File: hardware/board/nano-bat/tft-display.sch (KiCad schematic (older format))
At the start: 0 parts

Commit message: Adding larger microcontroller
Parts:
- added J?: Conn_2Rows-45Pins, symbol Connector_Generic:Conn_2Rows-45Pins
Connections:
- new net DB0: J?.28 (Pin_28)
- new net DB1: J?.27 (Pin_27)
- new net DB10: J?.18 (Pin_18)
- new net DB11: J?.17 (Pin_17)
- new net DB12: J?.16 (Pin_16)
- new net DB13: J?.15 (Pin_15)
- new net DB14: J?.14 (Pin_14)
- new net DB15: J?.13 (Pin_13)
- new net DB16: J?.12 (Pin_12)
- new net DB17: J?.11 (Pin_11)
- new net DB2: J?.26 (Pin_26)
- new net DB3: J?.25 (Pin_25)
- new net DB4: J?.24 (Pin_24)
- new net DB5: J?.23 (Pin_23)
- new net DB6: J?.22 (Pin_22)
- new net DB7: J?.21 (Pin_21)
- new net DB8: J?.20 (Pin_20)
- new net DB9: J?.19 (Pin_19)
- new net DOTCLK: J?.9 (Pin_9)
- new net ENABLE: J?.10 (Pin_10)
- new net FMARK: J?.35 (Pin_35)
- new net GND: J?.38 (Pin_38), J?.39 (Pin_39)
- new net HSYNC: J?.8 (Pin_8)
- new net IM0: J?.2 (Pin_2)
- new net IM1: J?.3 (Pin_3)
- new net IM2: J?.4 (Pin_4)
- new net IM3: J?.5 (Pin_5)
- new net LED_A: J?.40 (Pin_40)
- new net LED_K: J?.41 (Pin_41)
- new net RD: J?.31 (Pin_31)
- new net RESET: J?.6 (Pin_6)
- new net RS_SCL: J?.32 (Pin_32)
- new net SDI: J?.30 (Pin_30)
- new net SDO: J?.29 (Pin_29)
- new net VCC: J?.36 (Pin_36), J?.37 (Pin_37)
- new net VSYNC: J?.7 (Pin_7)
- new net WR: J?.33 (Pin_33)
- new net ~CS: J?.34 (Pin_34)
- no-connect marks 0 -> 5
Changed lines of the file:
@@
 $Descr A4 11693 8268
 encoding utf-8
-Sheet 1 6
-Title ""
+Sheet 4 6
+Title "NanoBat"
 Date ""
-Rev ""
-Comp ""
-Comment1 ""
+Rev "0.1.0"
+Comp "Vertigo Designs"
+Comment1 "Author: Ryan Summers"
 Comment2 ""
 Comment3 ""
 Comment4 ""
 $EndDescr
+$Comp
+L Connector_Generic:Conn_2Rows-45Pins J?
+U 1 1 5E7D047E
+P 5300 3850
+F 0 "J?" H 5350 5167 50  0000 C CNN
+F 1 "Conn_2Rows-45Pins" H 5350 5076 50  0000 C CNN
+F 2 "" H 5300 3850 50  0001 C CNN
+F 3 "~" H 5300 3850 50  0001 C CNN
+	1    5300 3850
+	1    0    0    -1
+$EndComp
+NoConn ~ 5100 2750
+NoConn ~ 5600 4750
+NoConn ~ 5600 4850
+NoConn ~ 5100 4850
+NoConn ~ 5100 4950
+Text Label 5700 2750 0    50   ~ 0
+IM0
+Text Label 5000 2850 2    50   ~ 0
+IM1
+Text Label 5000 2950 2    50   ~ 0
+IM3
+Text Label 5000 3050 2    50   ~ 0
+VSYNC
+Text Label 5000 3150 2    50   ~ 0
+DOTCLK
+Text Label 5700 3150 0    50   ~ 0
+ENABLE
+Text Label 5000 4150 2    50   ~ 0
+SDO
+Text Label 5000 4250 2    50   ~ 0
+RD
+Text Label 5000 4350 2    50   ~ 0
+WR
+Text Label 5000 4450 2    50   ~ 0
+FMARK
+Text Label 5000 4550 2    50   ~ 0
+VCC
+$Comp
+L power:GND #PWR?
+U 1 1 5E7D3FEB
+P 5000 5050
+F 0 "#PWR?" H 5000 4800 50  0001 C CNN
+F 1 "GND" H 5005 4877 50  0000 C CNN
+F 2 "" H 5000 5050 50  0001 C CNN
+F 3 "" H 5000 5050 50  0001 C CNN
+	1    5000 5050
+	1    0    0    -1
+$EndComp
+Wire Wire Line
+	5000 5050 5000 4650
+Wire Wire Line
+	5000 4650 5100 4650
+Text Label 4950 4750 2    50   ~ 0
+LED_K
+Wire Wire Line
+	5100 4750 4950 4750
+Wire Wire Line
+	5100 4550 5000 4550
+Wire Wire Line
+	5100 4450 5000 4450
+Wire Wire Line
+	5100 4350 5000 4350
+Wire Wire Line
+	5100 4250 5000 4250
+Wire Wire Line
+	5100 4150 5000 4150
+Text Label 5700 2850 0    50   ~ 0
+IM2
+Text Label 5700 2950 0    50   ~ 0
+RESET
+Text Label 5700 3050 0    50   ~ 0
+HSYNC
+Text Label 5700 4150 0    50   ~ 0
+SDI
+Text Label 5700 4250 0    50   ~ 0
+RS_SCL
+Text Label 5700 4350 0    50   ~ 0
+~CS
+Text Label 5700 4450 0    50   ~ 0
+VCC
+$Comp
+L power:GND #PWR?
+U 1 1 5E7D5AE2
+P 5700 5100
+F 0 "#PWR?" H 5700 4850 50  0001 C CNN
+F 1 "GND" H 5705 4927 50  0000 C CNN
+F 2 "" H 5700 5100 50  0001 C CNN
+F 3 "" H 5700 5100 50  0001 C CNN
+	1    5700 5100
+	1    0    0    -1
+$EndComp
+Wire Wire Line
+	5700 5100 5700 4550
+Wire Wire Line
+	5700 4550 5600 4550
+Text Label 5750 4650 0    50   ~ 0
+LED_A
+Wire Wire Line
+	5750 4650 5600 4650
+Wire Wire Line
+	5700 4450 5600 4450
+Wire Wire Line
+	5700 4350 5600 4350
+Wire Wire Line
+	5700 4250 5600 4250
+Wire Wire Line
+	5700 4150 5600 4150
+Text Label 5000 3250 2    50   ~ 0
+DB17
+Text Label 5000 3350 2    50   ~ 0
+DB15
+Text Label 5000 3450 2    50   ~ 0
+DB13
+Text Label 5000 3550 2    50   ~ 0
+DB11
+Text Label 5000 3650 2    50   ~ 0
+DB9
+Text Label 5000 3750 2    50   ~ 0
+DB7
+Text Label 5000 3850 2    50   ~ 0
+DB5
+Text Label 5000 3950 2    50   ~ 0
+DB3
+Text Label 5000 4050 2    50   ~ 0
+DB1
+Text Label 5700 3250 0    50   ~ 0
+DB16
+Text Label 5700 3350 0    50   ~ 0
+DB14
+Text Label 5700 3450 0    50   ~ 0
+DB12
+Text Label 5700 3550 0    50   ~ 0
+DB10
+Text Label 5700 3650 0    50   ~ 0
+DB8
+Text Label 5700 3750 0    50   ~ 0
+DB6
+Text Label 5700 3850 0    50   ~ 0
+DB4
+Text Label 5700 3950 0    50   ~ 0
+DB2
+Text Label 5700 4050 0    50   ~ 0
+DB0
+Wire Wire Line
+	5700 4050 5600 4050
+Wire Wire Line
+	5700 3950 5600 3950
+Wire Wire Line
+	5700 3850 5600 3850
+Wire Wire Line
+	5700 3750 5600 3750
+Wire Wire Line
+	5700 3650 5600 3650
+Wire Wire Line
+	5700 3550 5600 3550
+Wire Wire Line
+	5700 3450 5600 3450
+Wire Wire Line
+	5700 3350 5600 3350
+Wire Wire Line
+	5700 3250 5600 3250
+Wire Wire Line
+	5700 3150 5600 3150
+Wire Wire Line
+	5700 3050 5600 3050
+Wire Wire Line
+	5700 2950 5600 2950
+Wire Wire Line
+	5700 2850 5600 2850
+Wire Wire Line
+	5700 2750 5600 2750
+Wire Wire Line
+	5000 2850 5100 2850
+Wire Wire Line
+	5000 2950 5100 2950
+Wire Wire Line
+	5000 3050 5100 3050
+Wire Wire Line
+	5000 3150 5100 3150
+Wire Wire Line
+	5000 3250 5100 3250
+Wire Wire Line
+	5000 3350 5100 3350
+Wire Wire Line
+	5000 3450 5100 3450
+Wire Wire Line
+	5000 3550 5100 3550
+Wire Wire Line
+	5000 3650 5100 3650
+Wire Wire Line
+	5000 3750 5100 3750
+Wire Wire Line
+	5000 3850 5100 3850
+Wire Wire Line
+	5000 3950 5100 3950
+Wire Wire Line
+	5000 4050 5100 4050
 $EndSCHEMATC

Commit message: Adding WIP before reverting
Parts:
- added C?: 4.7u, symbol Device:C
- added C?: 1u, symbol Device:C
- added D?: D_Schottky, symbol Device:D_Schottky
- added L?: 6.8u, symbol Device:L
- added R?: 10, symbol Device:R_US
- added U?: AP3032, symbol nano-bat:AP3032
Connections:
- net labels added: +2V8, BL_CNTRL, D~CX, SCL
- net labels removed: DB0, DB1, DB10, DB11, DB12, DB13, DB14, DB15, DB16, DB17, DB2, DB3, DB4, DB5, DB6, DB7, DB8, DB9, DOTCLK, ENABLE, HSYNC, RD, RS_SCL, VCC, VSYNC, WR
- wire segments 42 -> 100
- no-connect marks 5 -> 6

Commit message: Adding first-pass revisions and annotations, part selection
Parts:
- removed C?: 4.7u, symbol Device:C
- removed C?: 1u, symbol Device:C
- removed D?: D_Schottky, symbol Device:D_Schottky
- added C201: 0.1u, Capacitor_SMD:C_0603_1608Metric, symbol Device:C
- added C202: 1u, Capacitor_SMD:C_0603_1608Metric, symbol Device:C
- added D201: D_Schottky_ALT, Diode_SMD:D_SOD-323, symbol Device:D_Schottky_ALT
- J201: renamed from J?; footprint (none) -> Connector_FFC-FPC:Hirose_FH12-45S-0.5SH_1x45-1MP_P0.50mm_Horizontal; Part (none) -> HFA145CT-ND
- L201: renamed from L?; footprint (none) -> Inductor_SMD:L_0805_2012Metric; Part (none) -> 445-6761-1-ND
- R201: renamed from R?; footprint (none) -> Resistor_SMD:R_0603_1608Metric; Part (none) -> 311-10.0HRCT-ND
- U201: renamed from U?; footprint (none) -> Package_TO_SOT_SMD:SOT-23-6; Part (none) -> AP3032KTR-G1DICT-ND
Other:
- moved on the sheet: L201, R201, U201

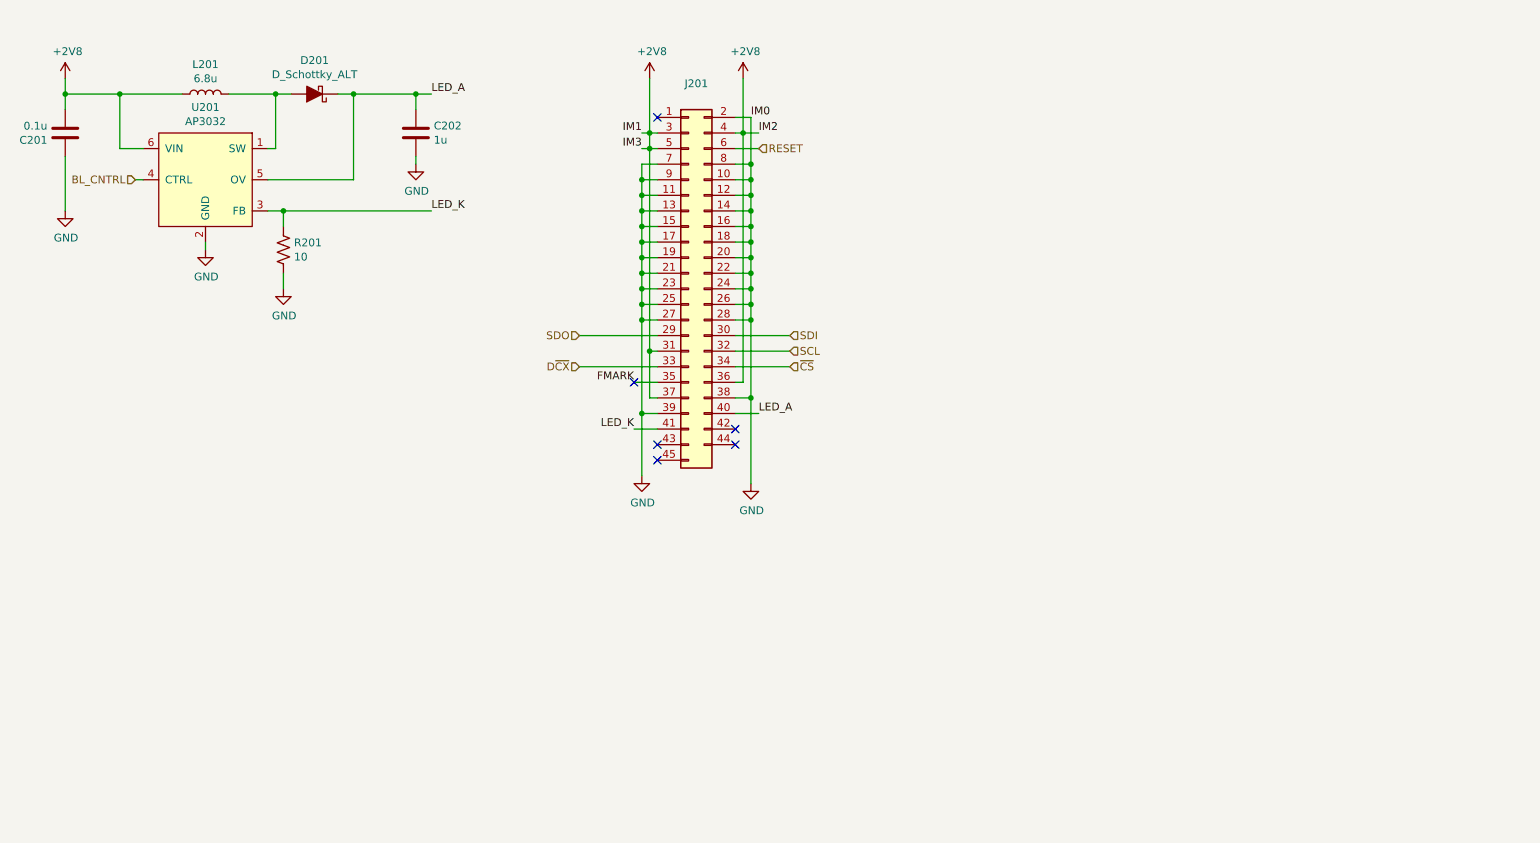
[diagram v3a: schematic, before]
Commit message: Adding 3D models, reorg, minor schematic fixes
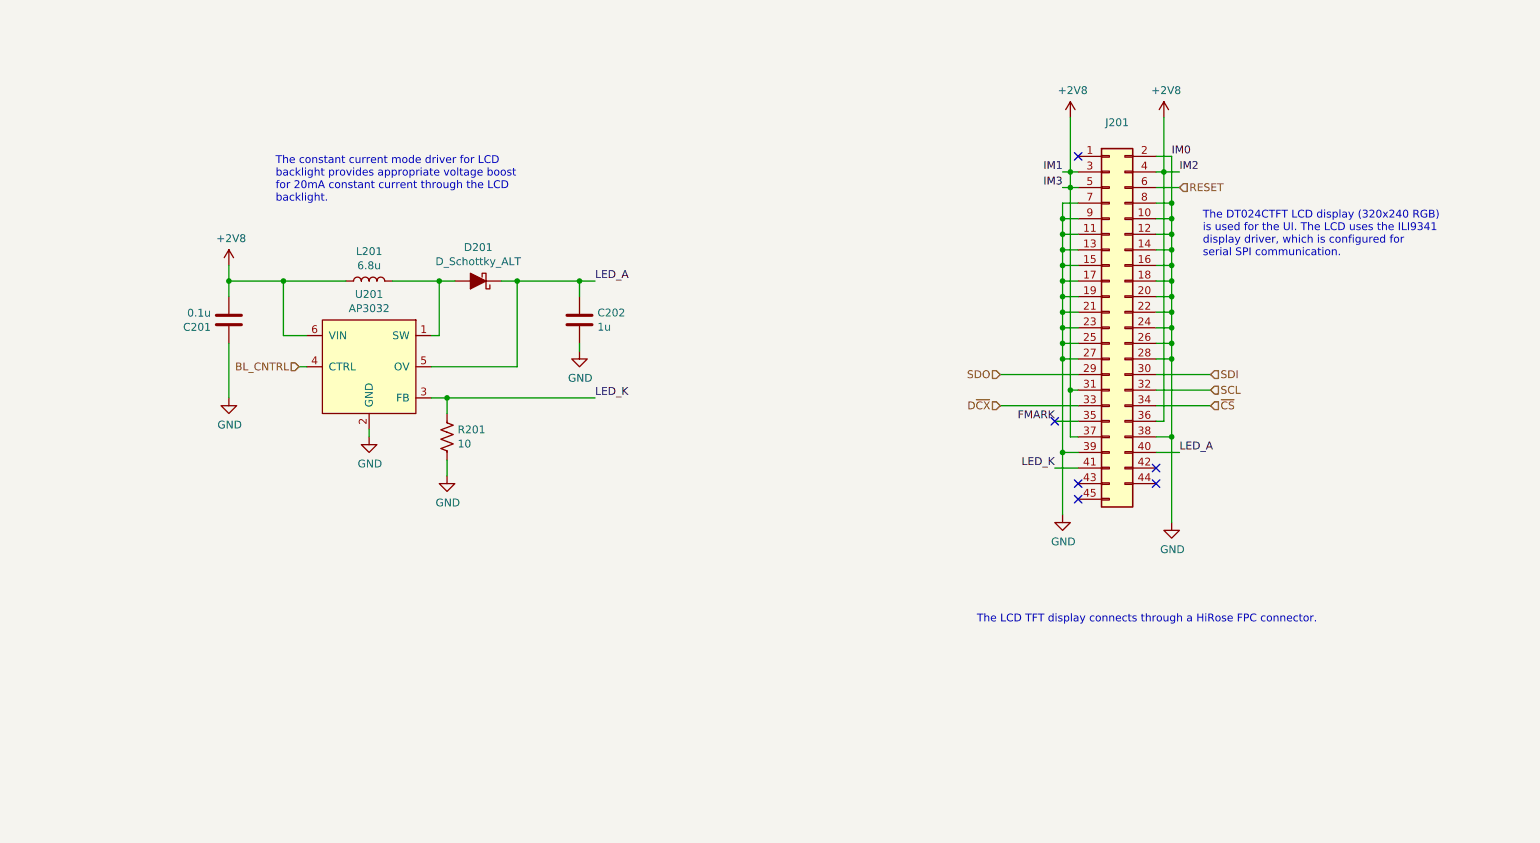
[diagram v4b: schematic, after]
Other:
- note added: "The DT024CTFT LCD display (320x240 RGB) \nis used for the UI. The LCD uses the ILI9341 \ndisplay driver, which is configured for\nserial SPI communication."
- note added: "The LCD TFT display connects through a HiRose FPC connector."
- note added: "The constant current mode driver for LCD \nbacklight provides appropriate voltage boost \nfor 20mA constant current through the LCD \nbacklight."
- moved on the sheet: C201, C202, D201, J201, L201, R201, U201

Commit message: Adding docs to schematic
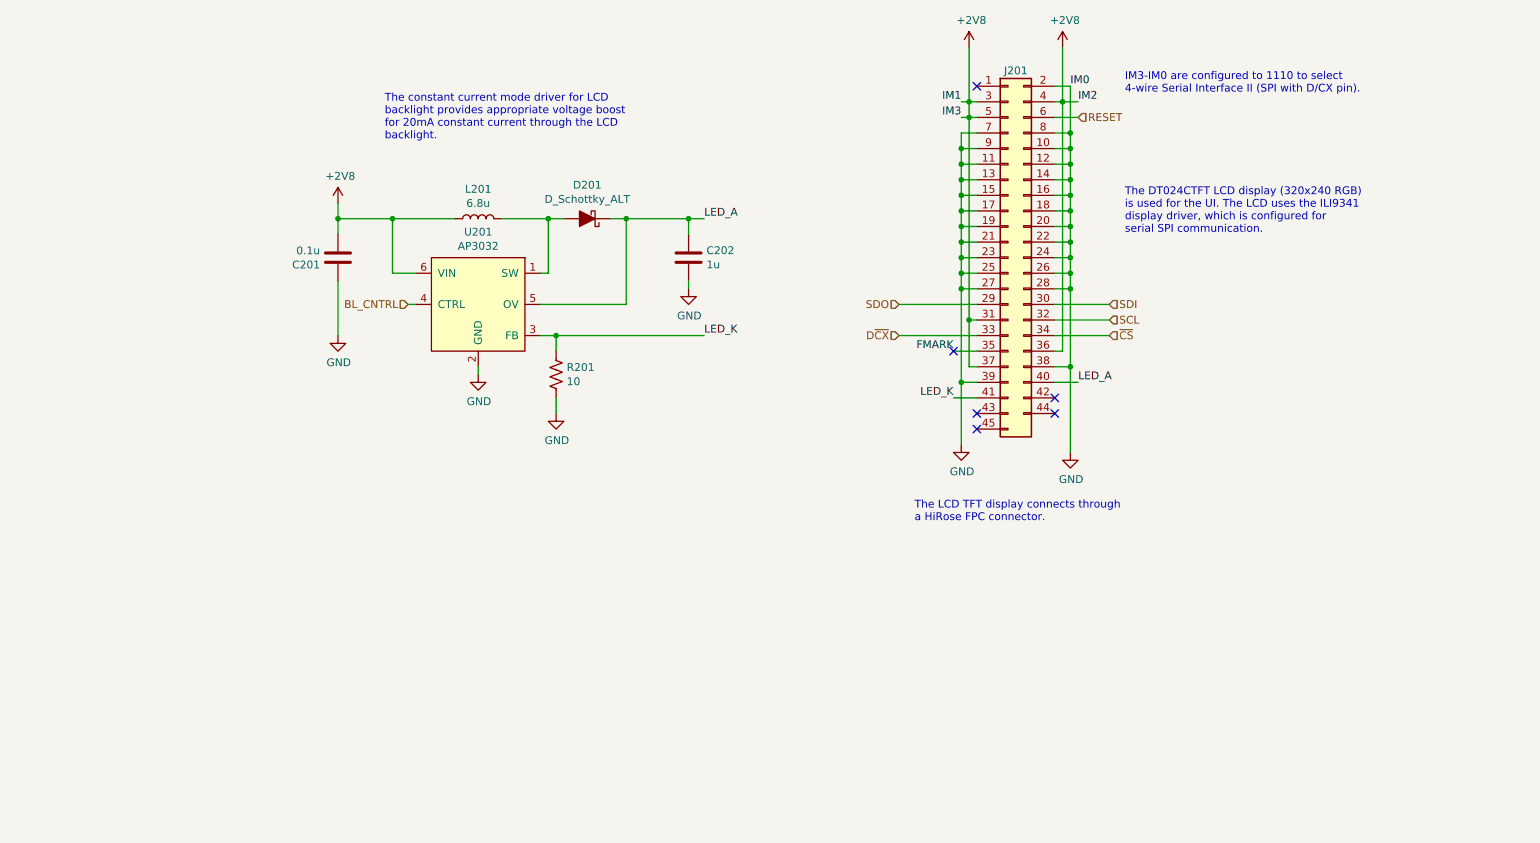
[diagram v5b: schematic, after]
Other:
- note added: "IM3-IM0 are configured to 1110 to select \n4-wire Serial Interface II (SPI with D/CX pin)."
- note added: "The LCD TFT display connects through \na HiRose FPC connector."
- note removed: "The LCD TFT display connects through a HiRose FPC connector."
- moved on the sheet: C201, C202, D201, J201, L201, R201, U201
